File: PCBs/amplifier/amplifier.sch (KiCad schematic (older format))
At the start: 47 parts, among them Q1 BC550, Q2 BC550, Q3 BD139, U1 LM337_TO220

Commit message: updated to kicad 5.
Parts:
- C1, C10, C2, C4, C6: symbol CP -> amplifier-rescue:CP
- C3, C5, C7, C8, C9: symbol C -> amplifier-rescue:C
- D1: symbol LED -> amplifier-rescue:LED
- D2: symbol D -> amplifier-rescue:D
- JP1: symbol Jumper -> amplifier-rescue:Jumper
- Q1, Q2: symbol BC550 -> amplifier-rescue:BC550
- Q3: symbol BD139 -> amplifier-rescue:BD139
- R1, R10, R11, R12, R13, R14, R15, R16, R17, R18, R19, R2, R20, R21, R22, R23, R24, R25, R3, R4, R5, R6, R7, R8, R9: symbol R -> amplifier-rescue:R
- RV1, RV2, RV3: symbol POT -> amplifier-rescue:POT
- U1: symbol LM337_TO220 -> amplifier-rescue:LM337_TO220
- V1: symbol ECC88 -> amplifier-rescue:ECC88
- V2: symbol ECC83 -> amplifier-rescue:ECC83
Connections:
- wire segments 75 -> 111

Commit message: fixed schematic.
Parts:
- C1: symbol amplifier-rescue:CP -> Device:C
- C10, C2, C4, C6: symbol amplifier-rescue:CP -> Device:CP
- C3, C5, C7, C8, C9: symbol amplifier-rescue:C -> Device:C
- D1: symbol amplifier-rescue:LED -> Device:LED
- D2: symbol amplifier-rescue:D -> Device:D
- JP1: symbol amplifier-rescue:Jumper -> Device:Jumper
- Q1, Q2: symbol amplifier-rescue:BC550 -> Transistor_BJT:BC550
- Q3: symbol amplifier-rescue:BD139 -> Transistor_BJT:BD139
- R1, R10, R11, R12, R13, R14, R15, R16, R17, R18, R19, R2, R20, R21, R22, R23, R24, R25, R3, R4, R5, R6, R7, R8, R9: symbol amplifier-rescue:R -> Device:R
- RV1, RV2, RV3: symbol amplifier-rescue:POT -> Device:POT
- U1: symbol amplifier-rescue:LM337_TO220 -> Regulator_Linear:LM337_TO220
- V1: symbol amplifier-rescue:ECC88 -> Valve:ECC88
- V2: symbol amplifier-rescue:ECC83 -> Valve:ECC83
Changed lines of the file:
@@
 $EndDescr
 $Comp
-L amplifier-rescue:ECC88 V1
+L Valve:ECC88 V1
 U 1 1 5AC23A79
 P 3800 3350
@@
 $EndComp
 $Comp
-L amplifier-rescue:ECC88 V1
-U 2 1 5AC23AD8
+L Valve:ECC88 V1
+U 0 1 5AC23AD8
 P 3150 3350
 F 0 "V1" H 3320 3630 50  0000 L CNN
@@
 F 2 "Valves:VALVE-NOVAL_P" H 3420 2950 50  0001 C CNN
 F 3 "" H 3150 3350 50  0001 C CNN
-	2    3150 3350
-	1    0    0    -1
-$EndComp
-$Comp
-L amplifier-rescue:ECC88 V1
-U 3 1 5AC23B39
+	0    3150 3350
+	1    0    0    -1
+$EndComp
+$Comp
+L Valve:ECC88 V1
+U 0 1 5AC23B39
 P 10050 2950
 F 0 "V1" H 10220 3230 50  0000 L CNN
@@
 F 2 "Valves:VALVE-NOVAL_P" H 10320 2550 50  0001 C CNN
 F 3 "" H 10050 2950 50  0001 C CNN
-	3    10050 2950
-	1    0    0    -1
-$EndComp
-$Comp
-L amplifier-rescue:ECC83 V2
+	0    10050 2950
+	1    0    0    -1
+$EndComp
+$Comp
+L Valve:ECC83 V2
 U 1 1 5AC23BC0
 P 4850 2900
@@
 $EndComp
 $Comp
-L amplifier-rescue:ECC83 V2
-U 2 1 5AC23C29
+L Valve:ECC83 V2
+U 0 1 5AC23C29
 P 9250 1700
 F 0 "V2" H 9380 2010 50  0000 C CNN
@@
 F 2 "Valves:VALVE-NOVAL_P" H 9520 1300 50  0001 C CNN
 F 3 "" H 9250 1700 50  0001 C CNN
-	2    9250 1700
-	1    0    0    -1
-$EndComp
-$Comp
-L amplifier-rescue:ECC83 V2
-U 3 1 5AC23C74
+	0    9250 1700
+	1    0    0    -1
+$EndComp
+$Comp
+L Valve:ECC83 V2
+U 0 1 5AC23C74
 P 10000 1650
 F 0 "V2" H 10130 1960 50  0000 C CNN
@@
 F 2 "Valves:VALVE-NOVAL_P" H 10270 1250 50  0001 C CNN
 F 3 "" H 10000 1650 50  0001 C CNN
-	3    10000 1650
-	1    0    0    -1
-$EndComp
-$Comp
-L amplifier-rescue:R R6
+	0    10000 1650
+	1    0    0    -1
+$EndComp
+$Comp
+L Device:R R6
 U 1 1 5AC23E18
 P 3150 2700
@@
 $EndComp
 $Comp
-L amplifier-rescue:R R9
+L Device:R R9
 U 1 1 5AC24148
 P 3800 2700
@@
 $EndComp
 $Comp
-L amplifier-rescue:R R11
+L Device:R R11
 U 1 1 5AC2419C
 P 4350 2900
@@
 $EndComp
 $Comp
-L amplifier-rescue:R R3
+L Device:R R3
 U 1 1 5AC24207
 P 2400 3350
@@
 $EndComp
 $Comp
-L amplifier-rescue:R R1
+L Device:R R1
 U 1 1 5AC242C7
 P 2100 3600
@@
 $EndComp
 $Comp
-L amplifier-rescue:R R10
+L Device:R R10
 U 1 1 5AC24344
 P 4150 3550
@@
 $EndComp
 $Comp
-L amplifier-rescue:R R13
+L Device:R R13
 U 1 1 5AC243E8
 P 4750 3550
@@
 $EndComp
 $Comp
-L amplifier-rescue:R R12
+L Device:R R12
 U 1 1 5AC2443D
 P 4550 1850
@@
 $EndComp
 $Comp
-L amplifier-rescue:R R5
+L Device:R R5
 U 1 1 5AC244FB
 P 2750 4250
@@
 $EndComp
 $Comp
-L amplifier-rescue:R R2
+L Device:R R2
 U 1 1 5AC2457A
 P 2100 5650
@@
 $EndComp
 $Comp
-L amplifier-rescue:R R4
+L Device:R R4
 U 1 1 5AC245EC
 P 2500 5650
@@
 $EndComp
 $Comp
-L amplifier-rescue:R R8
+L Device:R R8
 U 1 1 5AC24637
 P 3550 5700
@@
 $EndComp
 $Comp
-L amplifier-rescue:R R7
+L Device:R R7
 U 1 1 5AC24697
 P 3550 5300
@@
 $EndComp
 $Comp
-L amplifier-rescue:R R14
+L Device:R R14
 U 1 1 5AC246EE
 P 5150 5000
@@
 $EndComp
 $Comp
-L amplifier-rescue:R R18
+L Device:R R18
 U 1 1 5AC2478C
 P 6000 5050
@@
 $EndComp
 $Comp
-L amplifier-rescue:R R16
+L Device:R R16
 U 1 1 5AC247FB
 P 5650 5400
@@
 $EndComp
 $Comp
-L amplifier-rescue:R R15
+L Device:R R15
 U 1 1 5AC2488B
 P 5450 4400
@@
 $EndComp
 $Comp
-L amplifier-rescue:R R20
+L Device:R R20
 U 1 1 5AC248FE
 P 6100 4300
@@
 $EndComp
 $Comp
-L amplifier-rescue:R R25
+L Device:R R25
 U 1 1 5AC24996
 P 7200 3700
@@
 $EndComp
 $Comp
-L amplifier-rescue:R R24
+L Device:R R24
 U 1 1 5AC24A09
 P 7200 3200
@@
 $EndComp
 $Comp
-L amplifier-rescue:R R19
+L Device:R R19
 U 1 1 5AC24A77
 P 6050 2450
@@
 $EndComp
 $Comp
-L amplifier-rescue:R R22
+L Device:R R22
 U 1 1 5AC24B04
 P 6650 2200
@@
 $EndComp
 $Comp
-L amplifier-rescue:R R21
+L Device:R R21
 U 1 1 5AC24BA2
 P 6450 2900
@@
 $EndComp
 $Comp
-L amplifier-rescue:R R23
+L Device:R R23
 U 1 1 5AC24C23
 P 7000 1600
@@
 $EndComp
 $Comp
-L amplifier-rescue:R R17
+L Device:R R17
 U 1 1 5AC24CA1
 P 5700 1150
@@
 $EndComp
 $Comp
-L amplifier-rescue:C C5
+L Device:C C5
 U 1 1 5AC24D7E
 P 4550 2000
@@
 $EndComp
 $Comp
-L amplifier-rescue:CP C1
+L Device:C C1
 U 1 1 5AC24E35
 P 1700 2400
@@
 $EndComp
 $Comp
-L amplifier-rescue:C C7
+L Device:C C7
 U 1 1 5AC25250
 P 5350 2650
@@
 $EndComp
 $Comp
-L amplifier-rescue:C C3
+L Device:C C3
 U 1 1 5AC25A48
 P 3000 5600
@@
 $EndComp
 $Comp
-L amplifier-rescue:CP C2
+L Device:CP C2
 U 1 1 5AC25B19
 P 2750 5600
@@
 $EndComp
 $Comp
-L amplifier-rescue:LM337_TO220 U1
+L Regulator_Linear:LM337_TO220 U1
 U 1 1 5AC25F95
 P 4100 5100
@@
 $EndComp
 $Comp
-L amplifier-rescue:D D2
+L Device:D D2
 U 1 1 5AC262F5
 P 4050 4800
@@
 $EndComp
 $Comp
-L amplifier-rescue:CP C4
+L Device:CP C4
 U 1 1 5AC263D7
 P 4100 5700
@@
 $EndComp
 $Comp
-L amplifier-rescue:CP C6
+L Device:CP C6
 U 1 1 5AC266B3
 P 4650 5450
@@
 $EndComp
 $Comp
-L amplifier-rescue:BC550 Q1
+L Transistor_BJT:BC550 Q1
 U 1 1 5AC26A73
 P 3050 4050
@@
 $EndComp
 $Comp
-L amplifier-rescue:BC550 Q2
+L Transistor_BJT:BC550 Q2
 U 1 1 5AC26D0A
 P 3050 4500
@@
 $EndComp
 $Comp
-L amplifier-rescue:LED D1
+L Device:LED D1
 U 1 1 5AC27322
 P 2750 4800
@@
 $EndComp
 $Comp
-L amplifier-rescue:POT RV1
+L Device:POT RV1
 U 1 1 5AC275B6
 P 3150 4900
@@
 $EndComp
 $Comp
-L amplifier-rescue:GND #PWR01
+L power:GND #PWR01
 U 1 1 5AC2ED6E
 P 5350 2850
@@
 $EndComp
 $Comp
-L amplifier-rescue:Jumper JP1
+L Device:Jumper JP1
 U 1 1 5AC2FF11
 P 5100 1850
@@
 $EndComp
 $Comp
-L amplifier-rescue:C C8
+L Device:C C8
 U 1 1 5AC305F0
 P 5650 3100
@@
 $EndComp
 $Comp
-L amplifier-rescue:C C9
+L Device:C C9
 U 1 1 5AC306D0
 P 5650 3600
@@
 $EndComp
 $Comp
-L amplifier-rescue:POT RV2
+L Device:POT RV2
 U 1 1 5AC30773
 P 5850 3350
@@
 $EndComp
 $Comp
-L amplifier-rescue:BD139 Q3
+L Transistor_BJT:BD139 Q3
 U 1 1 5AC30809
 P 6250 3350
@@
 Connection ~ 5450 3350
 $Comp
-L amplifier-rescue:POT RV3
+L Device:POT RV3
 U 1 1 5AC321F1
 P 6250 2200
@@
 Connection ~ 6450 2200
 $Comp
-L amplifier-rescue:CP C10
+L Device:CP C10
 U 1 1 5AC32FC7
 P 6450 2400
@@
 $EndComp
 $Comp
-L amplifier-rescue:GND #PWR02
+L power:GND #PWR02
 U 1 1 5AC3357B
 P 6450 2600

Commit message: Raw finish of amp. schematic.
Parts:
- removed R17, R23: R, symbol Device:R
- removed V1: ECC88, Valves:VALVE-NOVAL_P, symbol Valve:ECC88
- removed V2: ECC83, Valves:VALVE-NOVAL_P, symbol Valve:ECC83
- added C? (x8): CP, symbol Device:CP
- added C? (x3): C, symbol Device:C
- added D? (x3): DIODE, symbol pspice:DIODE
- added D? (x3): 1N4148, Diode_THT:D_DO-35_SOD27_P7.62mm_Horizontal, symbol Diode:1N4148
- added J?: 6V3A, symbol Connector_Generic:Conn_01x01
- added J?: 6V3B, symbol Connector_Generic:Conn_01x01
- added K?: DIPxx-1Axx-11x, Relay_THT:Relay_StandexMeder_DIP_LowProfile, symbol Relay:DIPxx-1Axx-11x
- added LS?: Speaker, symbol Device:Speaker
- added Q?: 2SC2073, symbol Device:Q_NPN_BCE
- added Q? (x2): 2SC5200, symbol Device:Q_NPN_BCE
- added Q?: 2SA940, symbol Device:Q_PNP_BCE
- added Q?: 2SC1815, Package_TO_SOT_THT:TO-92_Inline, symbol Transistor_BJT:2SC1815
- added Q?: BS170, Package_TO_SOT_THT:TO-92_Inline, symbol Transistor_FET:BS170
- added Q? (x2): BC547, Package_TO_SOT_THT:TO-92_Inline, symbol Transistor_BJT:BC547
- added R? (x14): R, symbol Device:R
- added U?: LM317, symbol Regulator_Linear:LM317_3PinPackage
- added V1: ECC83, Valve:Valve_Noval_P, symbol Valve:ECC83
- added V2: ECC88, Valve:Valve_Noval_P, symbol Valve:ECC88
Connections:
- net labels added: +42V, -38V, FeedBack, RL-OUT, amp-out
- wire segments 111 -> 285
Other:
- moved on the sheet: C1, C10, C2, C3, C4, C5, C6, C7, C8, C9, D1, D2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

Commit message: Crude start of pcb.
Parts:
- K1: renamed from K?; value DIPxx-1Axx-11x -> LR-24
- U1: footprint TO_SOT_Packages_THT:TO-220_Vertical -> Package_TO_SOT_THT:TO-220-3_Vertical
- V1, V2: footprint Valve:Valve_Noval_P -> Valve:Valve_ECC-83-2
- gave numbers to parts that had none: 43

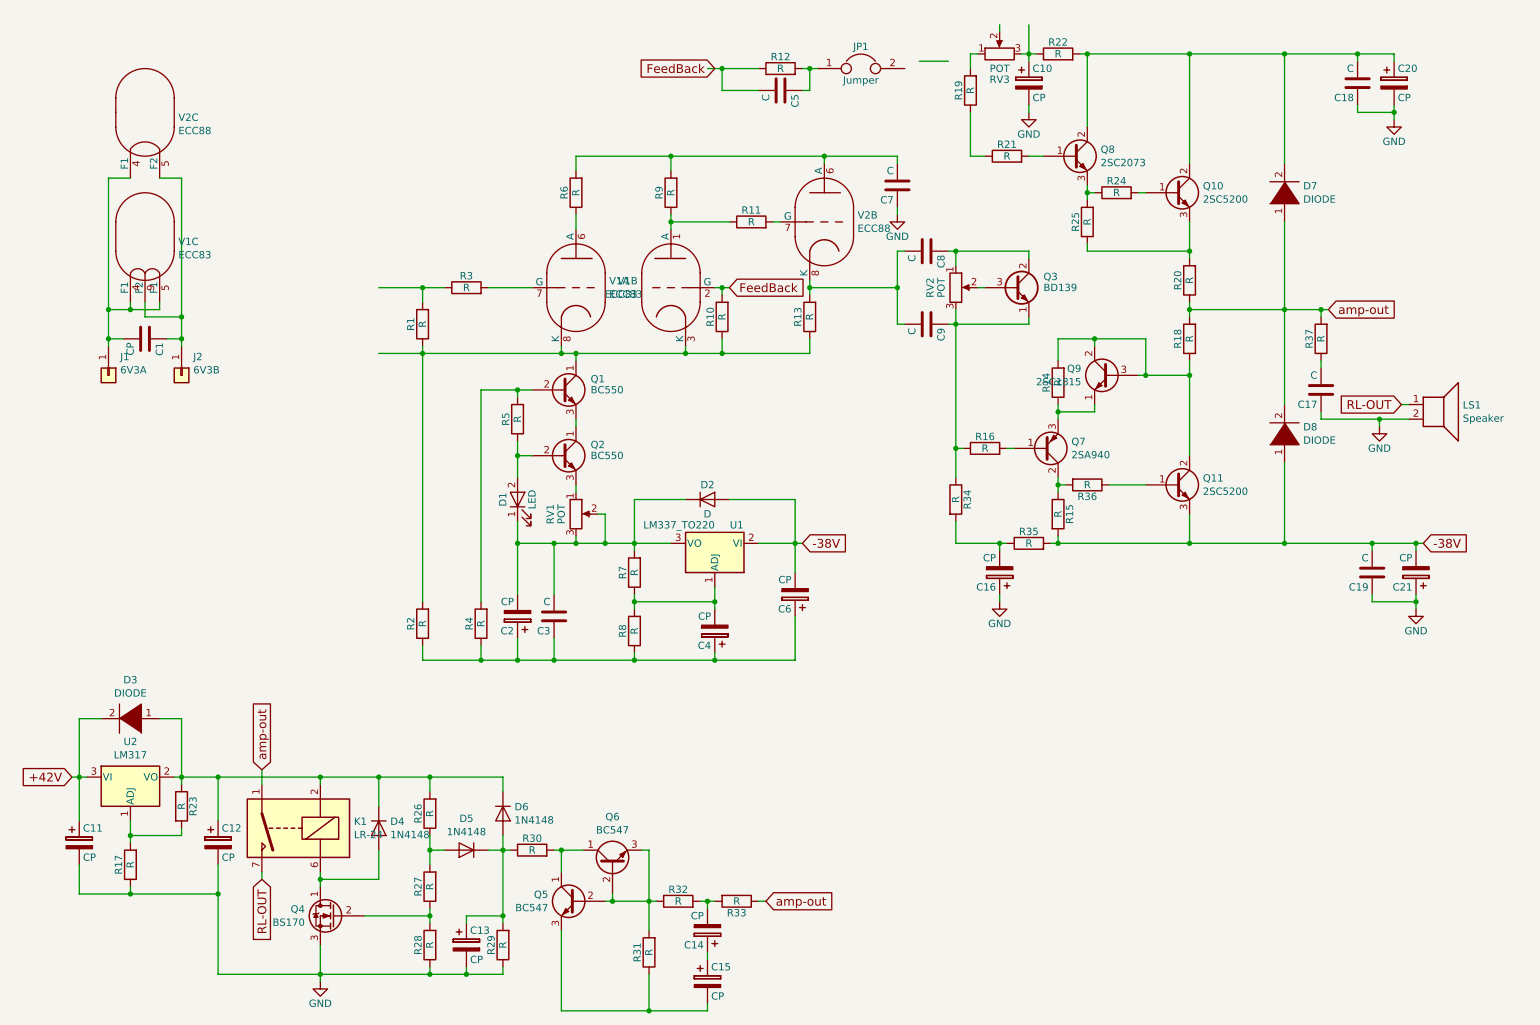
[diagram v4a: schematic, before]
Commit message: Added correct annotation and started assigning footprints.
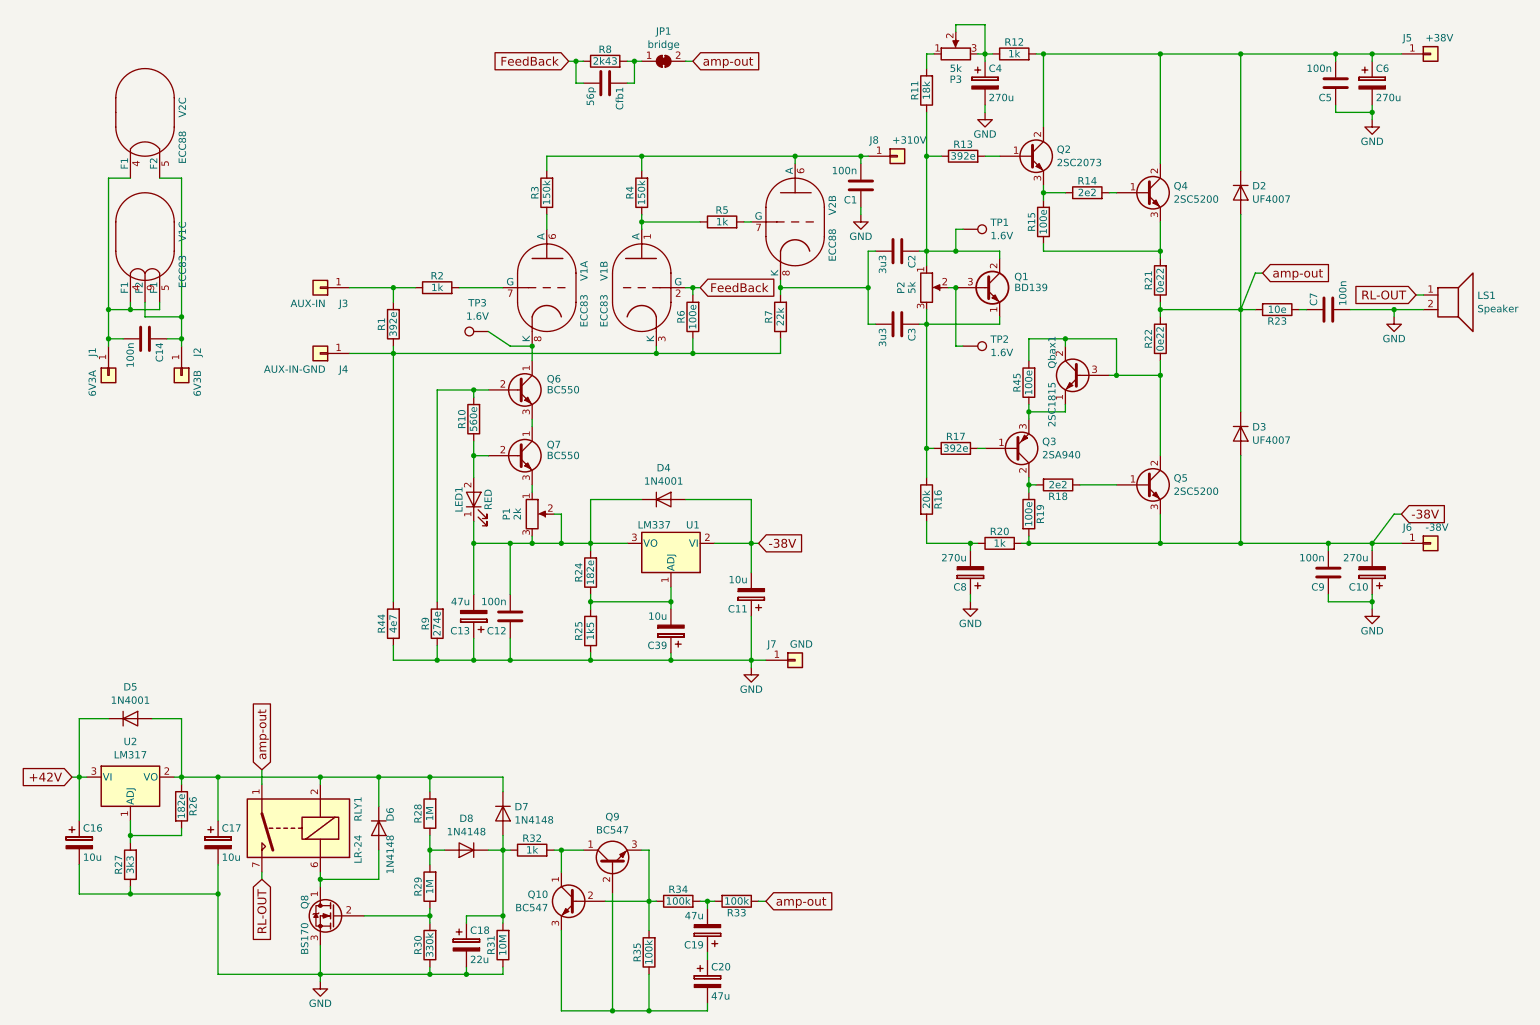
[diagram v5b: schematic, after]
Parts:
- removed D2: D, symbol Device:D
- removed D3, D7, D8: DIODE, symbol pspice:DIODE
- removed JP1: Jumper, symbol Device:Jumper
- added D2: UF4007, TestPoint:TestPoint_Pad_D1.0mm, symbol Diode:1N4007
- added D3: UF4007, Diode_THT:D_DO-41_SOD81_P10.16mm_Horizontal, symbol Diode:1N4007
- added D4, D5: 1N4001, Diode_THT:D_DO-41_SOD81_P10.16mm_Horizontal, symbol Diode:1N4001
- added J3: AUX-IN, symbol Connector_Generic:Conn_01x01
- added J4: AUX-IN-GND, symbol Connector_Generic:Conn_01x01
- added J5: +38V, symbol Connector_Generic:Conn_01x01
- added J6: -38V, symbol Connector_Generic:Conn_01x01
- added J7: GND, symbol Connector_Generic:Conn_01x01
- added J8: +310V, symbol Connector_Generic:Conn_01x01
- added JP1: bridge, symbol Jumper:SolderJumper_2_Bridged
- added TP1, TP2, TP3: 1.6V, TestPoint:TestPoint_Pad_D1.0mm, symbol Connector_Specialized:Test_Point
- C1: renamed from C7; value C -> 100n
- C10: renamed from C21; value CP -> 270u
- C11: renamed from C6; value CP -> 10u
- C12: renamed from C3; value C -> 100n
- C13: renamed from C2; value CP -> 47u
- C14: renamed from C1; value CP -> 100n
- C16: renamed from C11; value CP -> 10u
- C17: renamed from C12; value CP -> 10u
- C18: renamed from C13; value CP -> 22u
- C19: renamed from C14; value CP -> 47u
- C2: renamed from C8; value C -> 3u3
- C20: renamed from C15; value CP -> 47u
- C3: renamed from C9; value C -> 3u3
- C39: renamed from C4; value CP -> 10u
- C4: renamed from C10; value CP -> 270u
- C5: renamed from C18; value C -> 100n
- C6: renamed from C20; value CP -> 270u
- C7: renamed from C17; value C -> 100n
- C8: renamed from C16; value CP -> 270u
- C9: renamed from C19; value C -> 100n
- Cfb1: renamed from C5; value C -> 56p
- LED1: renamed from D1; value LED -> RED
- P1: renamed from RV1; value POT -> 2k; footprint (none) -> Potentiometer_THT:Potentiometer_ACP_CA14-H2,5_Horizontal
- P2: renamed from RV2; value POT -> 5k; footprint (none) -> Potentiometer_THT:Potentiometer_ACP_CA14-H2,5_Horizontal
- P3: renamed from RV3; value POT -> 5k; footprint (none) -> Potentiometer_THT:Potentiometer_ACP_CA14-H2,5_Horizontal
- Q4: renamed from Q10; footprint (none) -> Package_TO_SOT_THT:TO-264_Vertical
- Q5: renamed from Q11; footprint (none) -> Package_TO_SOT_THT:TO-264_Vertical
- R1: value R -> 392e; footprint (none) -> Resistor_THT:R_Axial_DIN0207_L6.3mm_D2.5mm_P7.62mm_Horizontal
- R10: renamed from R5; value R -> 560e; footprint (none) -> Resistor_THT:R_Axial_DIN0207_L6.3mm_D2.5mm_P7.62mm_Horizontal
- R11: renamed from R19; value R -> 18k; footprint (none) -> Resistor_THT:R_Axial_DIN0207_L6.3mm_D2.5mm_P7.62mm_Horizontal
- R12: renamed from R22; value R -> 1k; footprint (none) -> Resistor_THT:R_Axial_DIN0207_L6.3mm_D2.5mm_P7.62mm_Horizontal
- R13: renamed from R21; value R -> 392e; footprint (none) -> Resistor_THT:R_Axial_DIN0207_L6.3mm_D2.5mm_P7.62mm_Horizontal
- R14: renamed from R24; value R -> 2e2; footprint (none) -> Resistor_THT:R_Axial_DIN0207_L6.3mm_D2.5mm_P7.62mm_Horizontal
- R15: renamed from R25; value R -> 100e; footprint (none) -> Resistor_THT:R_Axial_DIN0207_L6.3mm_D2.5mm_P7.62mm_Horizontal
- R16: renamed from R34; value R -> 20k; footprint (none) -> Resistor_THT:R_Axial_DIN0207_L6.3mm_D2.5mm_P7.62mm_Horizontal
- R17: renamed from R16; value R -> 392e; footprint (none) -> Resistor_THT:R_Axial_DIN0207_L6.3mm_D2.5mm_P7.62mm_Horizontal
- R18: renamed from R36; value R -> 2e2; footprint (none) -> Resistor_THT:R_Axial_DIN0207_L6.3mm_D2.5mm_P7.62mm_Horizontal
- R19: renamed from R15; value R -> 100e; footprint (none) -> Resistor_THT:R_Axial_DIN0207_L6.3mm_D2.5mm_P7.62mm_Horizontal
- R2: renamed from R3; value R -> 1k; footprint (none) -> Resistor_THT:R_Axial_DIN0207_L6.3mm_D2.5mm_P7.62mm_Horizontal
- R20: renamed from R35; value R -> 1k; footprint (none) -> Resistor_THT:R_Axial_DIN0207_L6.3mm_D2.5mm_P7.62mm_Horizontal
- R21: renamed from R20; value R -> 0e22; footprint (none) -> Resistor_THT:R_Axial_Power_L25.0mm_W9.0mm_P27.94mm
- R22: renamed from R18; value R -> 0e22; footprint (none) -> Resistor_THT:R_Axial_Power_L25.0mm_W9.0mm_P27.94mm
- R23: renamed from R37; value R -> 10e; footprint (none) -> Resistor_THT:R_Axial_DIN0414_L11.9mm_D4.5mm_P15.24mm_Horizontal
- R24: renamed from R7; value R -> 182e; footprint (none) -> Resistor_THT:R_Axial_DIN0207_L6.3mm_D2.5mm_P7.62mm_Horizontal
- R25: renamed from R8; value R -> 1k5; footprint (none) -> Resistor_THT:R_Axial_DIN0207_L6.3mm_D2.5mm_P7.62mm_Horizontal
- R26: renamed from R23; value R -> 182e; footprint (none) -> Resistor_THT:R_Axial_DIN0207_L6.3mm_D2.5mm_P7.62mm_Horizontal
- R27: renamed from R17; value R -> 3k3; footprint (none) -> Resistor_THT:R_Axial_DIN0207_L6.3mm_D2.5mm_P7.62mm_Horizontal
- R28: renamed from R26; value R -> 1M; footprint (none) -> Resistor_THT:R_Axial_DIN0207_L6.3mm_D2.5mm_P7.62mm_Horizontal
- R29: renamed from R27; value R -> 1M; footprint (none) -> Resistor_THT:R_Axial_DIN0207_L6.3mm_D2.5mm_P7.62mm_Horizontal
- R3: renamed from R6; value R -> 150k; footprint (none) -> Resistor_THT:R_Axial_DIN0414_L11.9mm_D4.5mm_P15.24mm_Horizontal
- R30: renamed from R28; value R -> 330k; footprint (none) -> Resistor_THT:R_Axial_DIN0207_L6.3mm_D2.5mm_P7.62mm_Horizontal
- R31: renamed from R29; value R -> 10M; footprint (none) -> Resistor_THT:R_Axial_DIN0207_L6.3mm_D2.5mm_P7.62mm_Horizontal
- R32: renamed from R30; value R -> 1k; footprint (none) -> Resistor_THT:R_Axial_DIN0207_L6.3mm_D2.5mm_P7.62mm_Horizontal
- R33: value R -> 100k; footprint (none) -> Resistor_THT:R_Axial_DIN0207_L6.3mm_D2.5mm_P7.62mm_Horizontal
- R34: renamed from R32; value R -> 100k; footprint (none) -> Resistor_THT:R_Axial_DIN0207_L6.3mm_D2.5mm_P7.62mm_Horizontal
- R35: renamed from R31; value R -> 100k; footprint (none) -> Resistor_THT:R_Axial_DIN0207_L6.3mm_D2.5mm_P7.62mm_Horizontal
- R4: renamed from R9; value R -> 150k; footprint (none) -> Resistor_THT:R_Axial_DIN0414_L11.9mm_D4.5mm_P15.24mm_Horizontal
- R44: renamed from R2; value R -> 4e7; footprint (none) -> Resistor_THT:R_Axial_DIN0207_L6.3mm_D2.5mm_P7.62mm_Horizontal
- R45: renamed from R14; value R -> 100e; footprint (none) -> Resistor_THT:R_Axial_DIN0207_L6.3mm_D2.5mm_P7.62mm_Horizontal
- R5: renamed from R11; value R -> 1k; footprint (none) -> Resistor_THT:R_Axial_DIN0207_L6.3mm_D2.5mm_P7.62mm_Horizontal
- R6: renamed from R10; value R -> 100e; footprint (none) -> Resistor_THT:R_Axial_DIN0207_L6.3mm_D2.5mm_P7.62mm_Horizontal
- R7: renamed from R13; value R -> 22k; footprint (none) -> Resistor_THT:R_Axial_DIN0414_L11.9mm_D4.5mm_P15.24mm_Horizontal
- R8: renamed from R12; value R -> 2k43; footprint (none) -> Resistor_THT:R_Axial_DIN0207_L6.3mm_D2.5mm_P7.62mm_Horizontal
- R9: renamed from R4; value R -> 274e; footprint (none) -> Resistor_THT:R_Axial_DIN0207_L6.3mm_D2.5mm_P7.62mm_Horizontal
- U1: value LM337_TO220 -> LM337
- U2: footprint (none) -> Package_TO_SOT_THT:TO-220-3_Vertical
- renumbered D4 to D6, D6 to D7, D5 to D8, Q3 to Q1, Q5 to Q10, Q8 to Q2, Q7 to Q3, Q1 to Q6, Q2 to Q7, Q4 to Q8, Q6 to Q9, Q9 to Qbax1, K1 to RLY1
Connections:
- net +42V: now also D5.1 (K)
- net -38V: now also D3.2 (A), D4.2 (A), J6.1 (Pin_1)
- net GND: now also C11.1, C12.1, C13.1, C39.1, C7.2, R25.1, R44.1, R9.1, J7.1 (Pin_1); no longer C7.1
- net amp-out: now also D2.2 (A), D3.1 (K), JP1.2 (B)
- net at C1.2, R3.2, R4.2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: now also J8.1 (Pin_1)
- net at R1.2, R2.1: now also J3.1 (Pin_1)
- net at R1.1, R44.2, R6.1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: now also J4.1 (Pin_1); no longer Q6.1 (C), V1.8 (K)
- net at Cfb1.1, R8.2: now also JP1.1 (A)
- net at C12.2, C13.2, LED1.1 (K)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: now also D4.1 (K)
- net at R11.1, R13.1: now also C2.1, P2.1, Q1.2 (C), TP1.1
- net at C4.1, P3.3, R12.1: now also P3.2
- net at C5.2, C6.1, Q2.2 (C)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: now also D2.1 (K), J5.1 (Pin_1)
- net at P2.2, Q1.3 (B): now also TP2.1
- net at R23.1: now also C7.1; no longer C7.2
- net at C17.1, D6.1 (K), D7.1 (K)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: now also D5.2 (A)
- net at Q10.2 (B), Q9.3 (E), R34.1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: no longer Q9.2 (B)
- net at C20.2, Q10.3 (E), R35.1: now also Q9.2 (B)
- new net: Q6.1 (C), TP3.1, V1.8 (K)
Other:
- moved on the sheet: C1, C10, C11, C12, C13, C2, C3, C39, C4, C5, C6, C7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
